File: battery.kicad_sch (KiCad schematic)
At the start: 1 part, among them U2 BQ40z50-R2

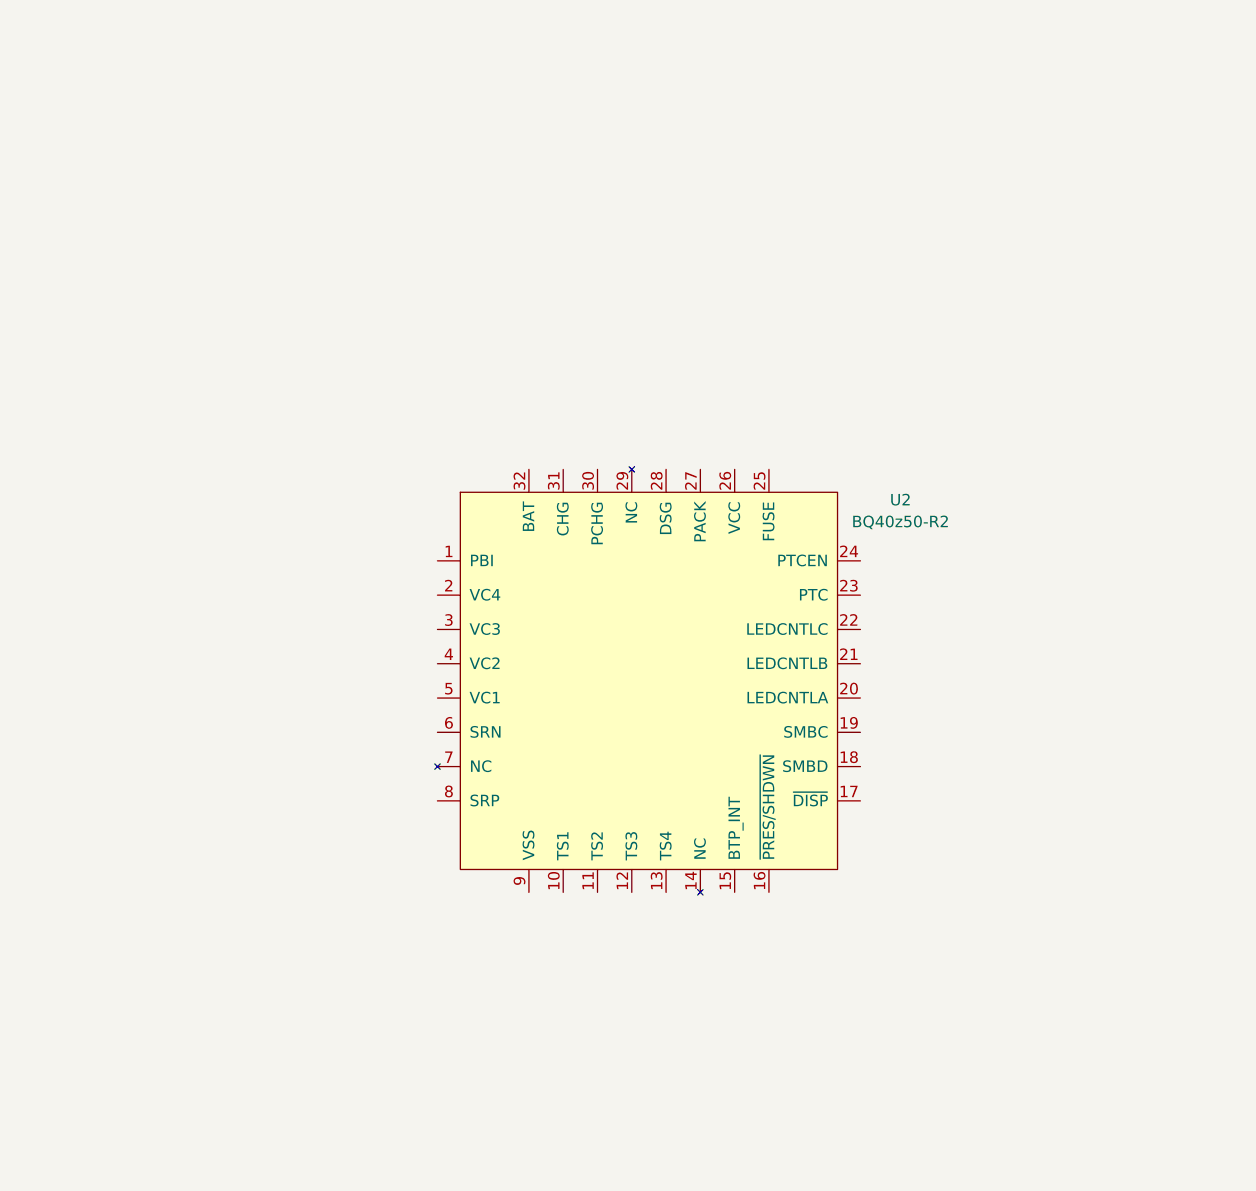
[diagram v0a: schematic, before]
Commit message: Add gauge schematic and partial charger schematic
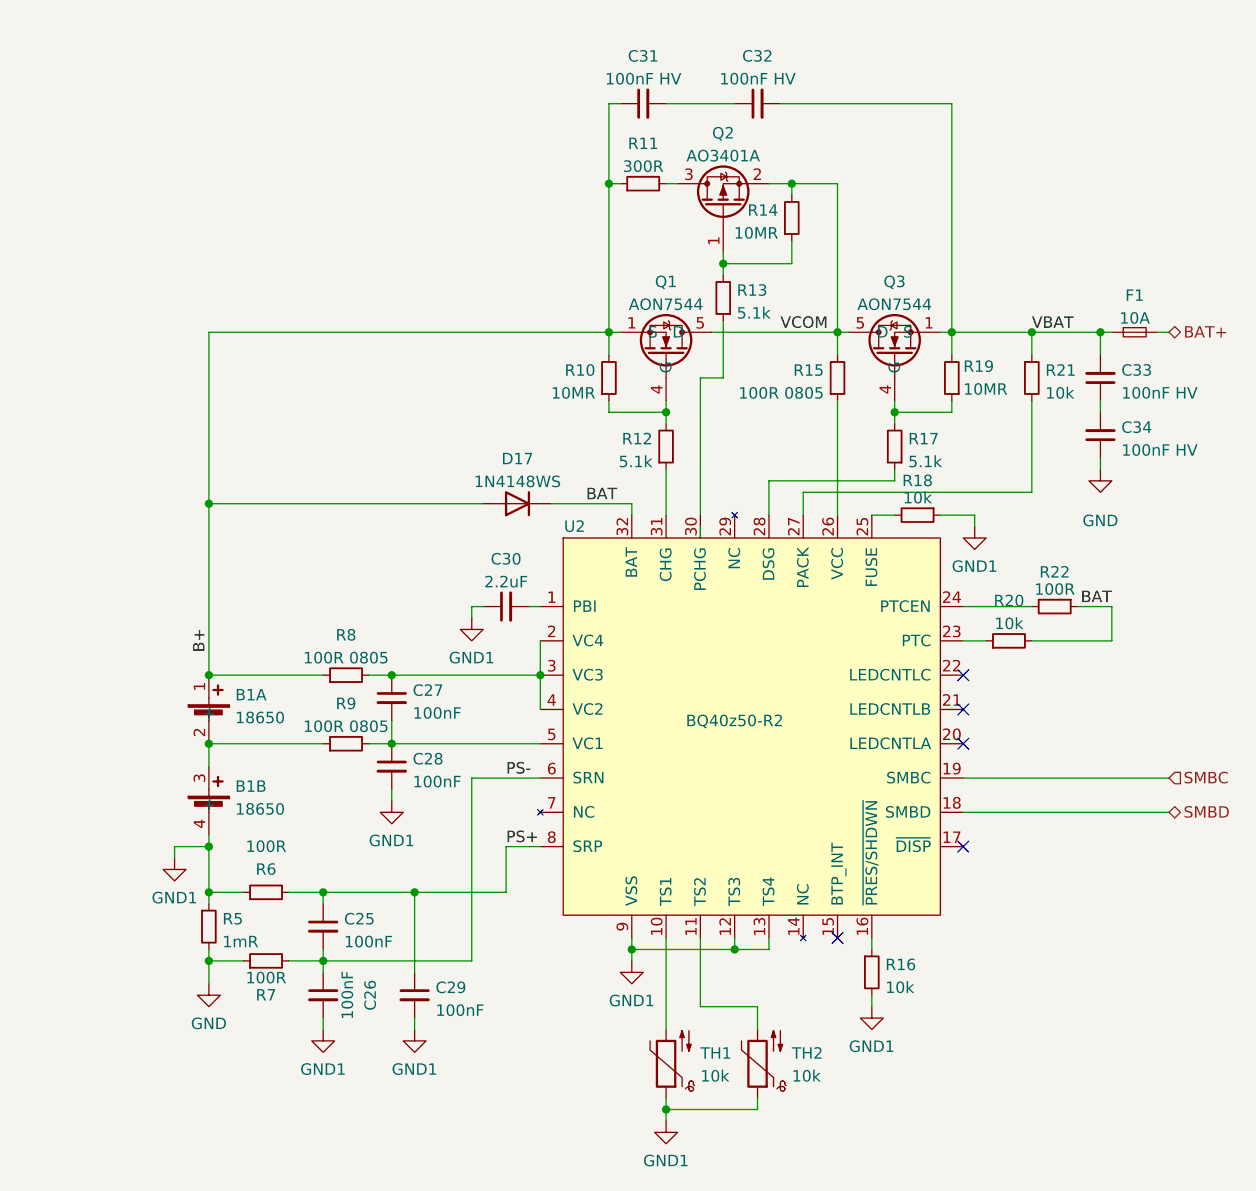
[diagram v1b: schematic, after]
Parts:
- added B1: 18650, symbol battery:battery-2s
- added C25, C26, C27, C28, C29: 100nF, Capacitor_SMD:C_0402_1005Metric, symbol Device:C_Small
- added C30: 2.2uF, Capacitor_SMD:C_0603_1608Metric, symbol Device:C_Small
- added C31, C32, C33, C34: 100nF HV, Capacitor_SMD:C_0603_1608Metric, symbol Device:C_Small
- added D17: 1N4148WS, Diode_SMD:D_SOD-323, symbol Diode:1N4148WS
- added F1: 10A, Fuse:Fuse_1206_3216Metric, symbol Device:Fuse_Small
- added Q1, Q3: AON7544, Package_DFN_FET:DFN-8-FET_3x3mm_P0.65mm, symbol Transistor_FET_DFN:AON7544
- added Q2: AO3401A, Package_TO_SOT_SMD:SOT-23, symbol Transistor_FET:AO3401A
- added R10, R14, R19: 10MR, Resistor_SMD:R_0402_1005Metric, symbol Device:R_Small
- added R11: 300R, Resistor_SMD:R_1206_3216Metric, symbol Device:R_Small
- added R12, R13, R17: 5.1k, Resistor_SMD:R_0402_1005Metric, symbol Device:R_Small
- added R15, R8, R9: 100R 0805, Resistor_SMD:R_0805_2012Metric, symbol Device:R_Small
- added R16, R18, R20, R21: 10k, Resistor_SMD:R_0402_1005Metric, symbol Device:R_Small
- added R22, R6, R7: 100R, Resistor_SMD:R_0402_1005Metric, symbol Device:R_Small
- added R5: 1mR, Resistor_SMD:R_1206_3216Metric, symbol Device:R_Small
- added TH1, TH2: 10k, Resistor_SMD:R_0402_1005Metric, symbol Device:Thermistor_NTC
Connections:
- net PWRPD is gone; now on net GND1: U2.33 (PWRPD), U2.9 (VSS)
- net at U2.1 (PBI): now also C30.2
- net at U2.10 (TS1): now also TH1.2
- net at U2.11 (TS2): now also TH2.2
- net GND1: now reaches U2.12 (TS3)
- net GND1: now also U2.13 (TS4), B1.4 (-), C26.2, C28.2, C29.2, C30.1, R16.2, R18.1, R5.1, R6.1, TH1.1, TH2.1
- net at U2.16 (~{PRES/SHDWN}): now also R16.1
- net SMBD: now reaches U2.18 (SMBD)
- net SMBC: now reaches U2.19 (SMBC)
- net at U2.2 (VC4): now also U2.3 (VC3), U2.4 (VC2), C27.1, R8.2
- net at U2.23 (PTC): now also R20.1
- net at U2.24 (PTCEN): now also R22.2
- net at U2.25 (FUSE): now also R18.2
- net at U2.26 (VCC): now also R15.1
- net at U2.27 (PACK): now also R21.2
- net at U2.28 (DSG): now also R17.1
- net at U2.30 (PCHG): now also R13.1
- net at U2.31 (CHG): now also R12.1
- net BAT: now reaches U2.32 (BAT)
- net BAT: now also D17.1 (K), R20.2, R22.1
- net at U2.5 (VC1): now also C27.2, C28.1, R9.2
- net PS-: now reaches U2.6 (SRN)
- net PS-: now also C25.2, C26.1, R7.2
- net PS+: now reaches U2.8 (SRP)
- net PS+: now also C25.1, C29.1, R6.2
- new net: C31.2, C32.1
- new net: Q2.1 (G), R13.2, R14.1
- new net: Q2.3 (D), R11.2
- new net: Q3.4 (G), R17.2, R19.1
- new net: Q1.4 (G), R10.1, R12.2
- new net: B1.2 (-), B1.3 (+), R9.1
- new net: C33.1, C34.2
- new net B+: B1.1 (+), C31.1, D17.2 (A), Q1.1 (S), Q1.2 (S), Q1.3 (S), R10.2, R11.1, R8.1
- new net BAT+: F1.2
- new net GND: C34.1, R5.2, R7.1
- new net VBAT: C32.2, C33.2, F1.1, Q3.1 (S), Q3.2 (S), Q3.3 (S), R19.2, R21.1
- new net VCOM: Q1.5 (D), Q1.6 (D), Q1.7 (D), Q1.8 (D), Q1.9 (D), Q2.2 (S), Q3.5 (D), Q3.6 (D), Q3.7 (D), Q3.8 (D), Q3.9 (D), R14.2, R15.2
- no-connect marks 0 -> 5

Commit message: Finish rough layout
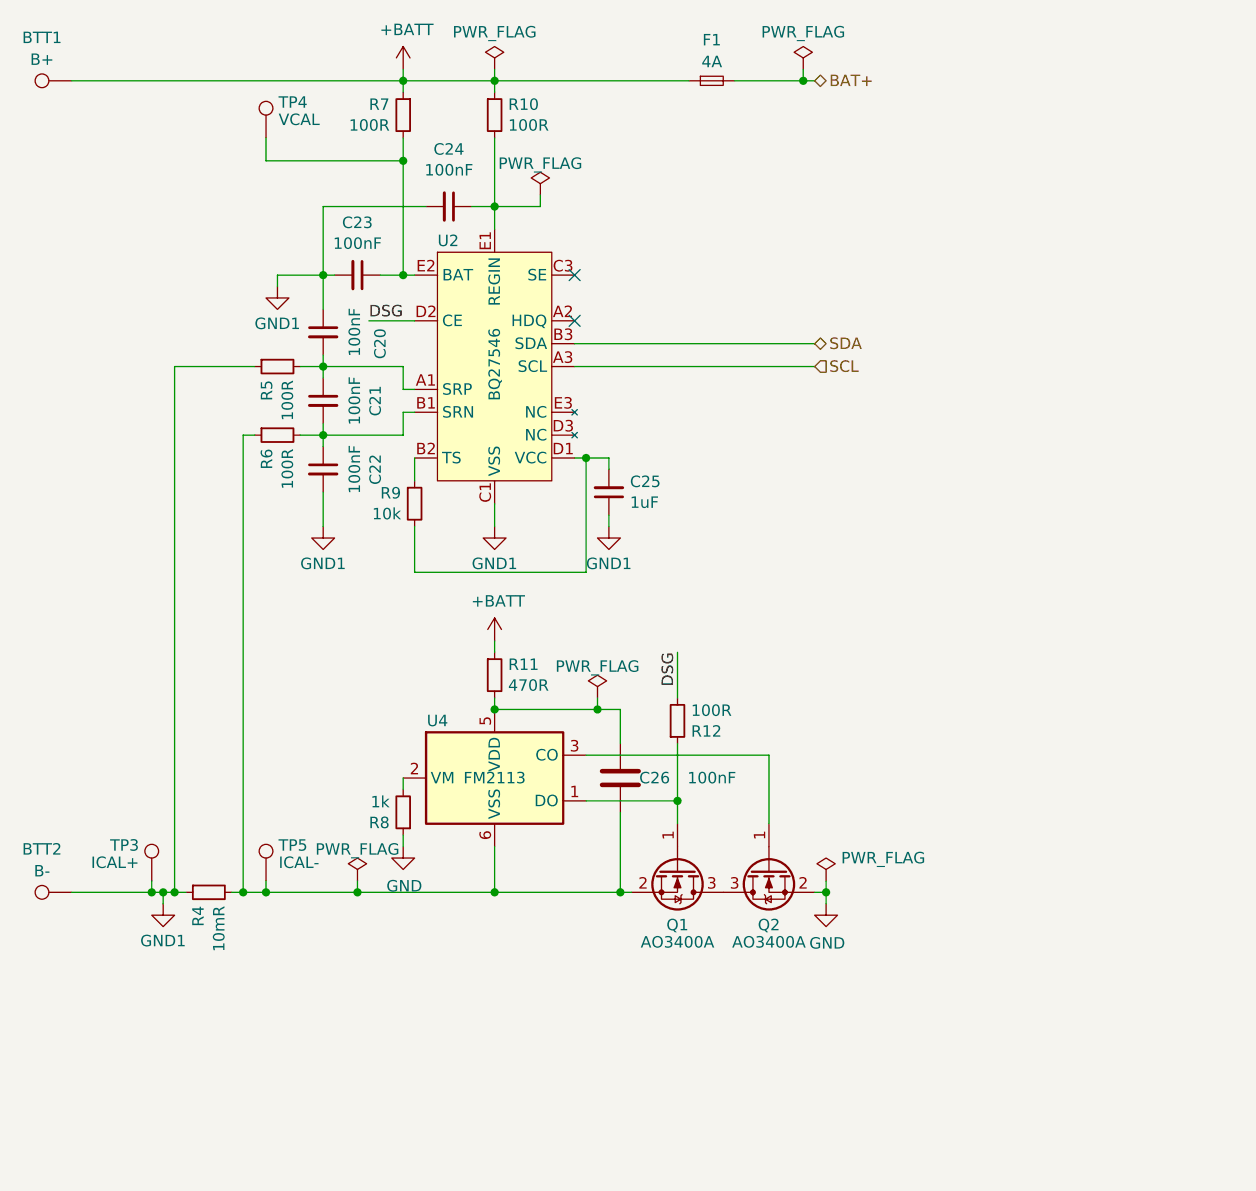
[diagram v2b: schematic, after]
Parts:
- removed B1: 18650, symbol battery:battery-2s
- removed C26, C27, C28, C29: 100nF, Capacitor_SMD:C_0402_1005Metric, symbol Device:C_Small
- removed C30: 2.2uF, Capacitor_SMD:C_0603_1608Metric, symbol Device:C_Small
- removed C31, C32, C33, C34: 100nF HV, Capacitor_SMD:C_0603_1608Metric, symbol Device:C_Small
- removed D17: 1N4148WS, Diode_SMD:D_SOD-323, symbol Diode:1N4148WS
- removed Q1, Q3: AON7544, Package_DFN_FET:DFN-8-FET_3x3mm_P0.65mm, symbol Transistor_FET_DFN:AON7544
- removed Q2: AO3401A, Package_TO_SOT_SMD:SOT-23, symbol Transistor_FET:AO3401A
- removed R13, R17: 5.1k, Resistor_SMD:R_0402_1005Metric, symbol Device:R_Small
- removed R14, R19: 10MR, Resistor_SMD:R_0402_1005Metric, symbol Device:R_Small
- removed R15: 100R 0805, Resistor_SMD:R_0805_2012Metric, symbol Device:R_Small
- removed R16, R18, R20, R21: 10k, Resistor_SMD:R_0402_1005Metric, symbol Device:R_Small
- removed R22: 100R, Resistor_SMD:R_0402_1005Metric, symbol Device:R_Small
- removed TH1, TH2: 10k, Resistor_SMD:R_0402_1005Metric, symbol Device:Thermistor_NTC
- removed U2: BQ40z50-R2, Package_Texas:VQFN-32-4.1x4.1-EP-1.4, symbol ti-balancers:BQ40z50-R2
- added BTT1: B+, Battery_Holder_MYOUNG:MY-18650-01, symbol Connector:TestPoint
- added BTT2: B-, Battery_Holder_MYOUNG:MY-18650-01, symbol Connector:TestPoint
- added C20, C21, C22, C23, C24: 100nF, Capacitor_SMD:C_0402_1005Metric, symbol Device:C_Small
- added C26: 100nF, Capacitor_SMD:C_0402_1005Metric, symbol Device:C
- added Q1, Q2: AO3400A, Package_TO_SOT_SMD:SOT-23, symbol Transistor_FET:AO3400A
- added R4: 10mR, Resistor_SMD:R_0805_2012Metric, symbol Device:R_Small
- added TP3: ICAL+, TestPoint:TestPoint_Pad_2.0x2.0mm, symbol Connector:TestPoint
- added TP4: VCAL, TestPoint:TestPoint_Pad_2.0x2.0mm, symbol Connector:TestPoint
- added TP5: ICAL-, TestPoint:TestPoint_Pad_1.5x1.5mm, symbol Connector:TestPoint
- added U2: BQ27546, Package_DSBGA:DSBGA-15_BQ27546_I2C_1.95x2.6mm_P0.5mm, symbol Fuel_Gauge_TI:BQ27546
- added U4: FM2113, Package_TO_SOT_SMD:SOT-23-6, symbol Battery_Management:AP9101CK6
- C25: value 100nF -> 1uF; LCSC C1525 -> C52923
- F1: value 10A -> 4A; LCSC C242475 -> C187596
- R10: value 10MR -> 100R; LCSC C26082 -> C25076
- R11: value 300R -> 470R; footprint Resistor_SMD:R_1206_3216Metric -> Resistor_SMD:R_0402_1005Metric; LCSC C17887 -> C25117
- R12: value 5.1k -> 100R; LCSC C25905 -> C25076
- R5: value 1mR -> 100R; footprint Resistor_SMD:R_1206_3216Metric -> Resistor_SMD:R_0402_1005Metric; LCSC C76287 -> C25076
- R8: value 100R 0805 -> 1k; footprint Resistor_SMD:R_0805_2012Metric -> Resistor_SMD:R_0402_1005Metric; LCSC C17408 -> C11702
- R9: value 100R 0805 -> 10k; footprint Resistor_SMD:R_0805_2012Metric -> Resistor_SMD:R_0402_1005Metric; LCSC C17408 -> C25744
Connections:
- net VBAT is gone; now on net +BATT: F1.1
- net GND: now also R8.1, Q2.2 (S); no longer R5.2, R7.1
- net GND1: now also C25.1, BTT2.1, C20.1, C22.2, C23.2, C24.2, R4.1, TP3.1, U2.C1 (VSS), U2.C2 (VSS); no longer R6.1
- net at R9.2: now also C25.2, U2.D1 (VCC)
- net at R11.2: now also C26.2, U4.5 (VDD)
- net +BATT: now reaches R10.1
- net +BATT: now also R11.1, R7.1, BTT1.1; no longer R12.2
- net at R9.1: now also U2.B2 (TS)
- net at R12.1: now also Q1.1 (G), U4.1 (DO)
- net at R8.2: now also U4.2 (VM)
- removed net B+: R10.2, R11.1, R8.1
- net PS+: no longer names the net of R6.2
- net PS+: now also C21.2, C22.1, U2.B1 (SRN); no longer C25.1
- net PS-: no longer names the net of R7.2
- net PS-: now also C23.1, TP4.1, U2.E2 (BAT); no longer C25.2
- new net: C26.1, Q1.2 (S), R4.2, R6.1, TP5.1, U4.6 (VSS)
- new net: C20.2, C21.1, R5.2, U2.A1 (SRP)
- new net: Q2.1 (G), U4.3 (CO)
- new net: C24.1, R10.2, U2.E1 (REGIN)
- new net: Q1.3 (D), Q2.3 (D)
- new net DSG: R12.2, U2.D2 (CE)
- new net SCL: U2.A3 (SCL)
- new net SDA: U2.B3 (SDA)
- no-connect marks 5 -> 2

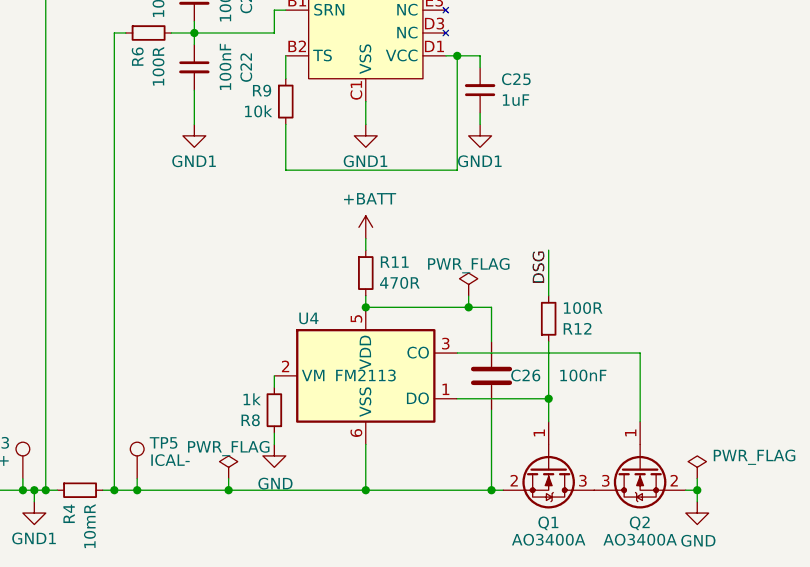
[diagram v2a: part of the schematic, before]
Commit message: Reduce battery protection IC VDD impedance
Reduce from 470R to 100R in line with manufacturers recommendation
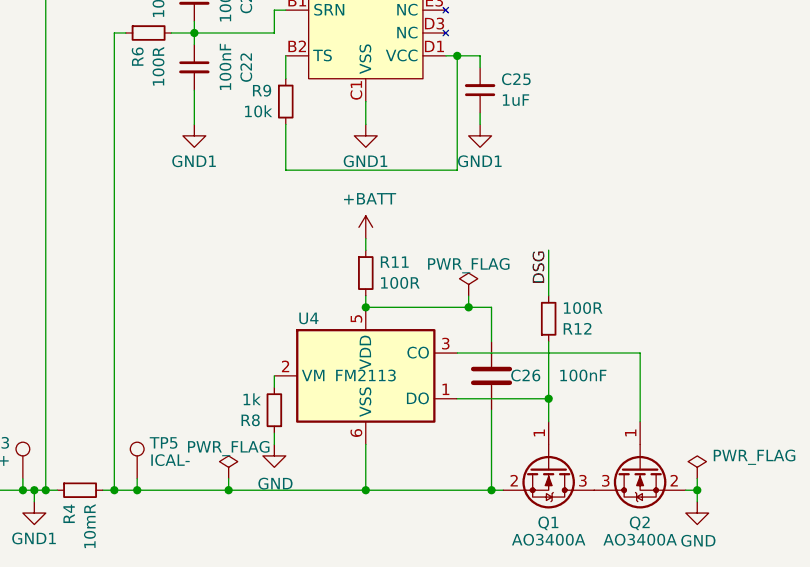
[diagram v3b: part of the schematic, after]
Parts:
- Q1, Q2: LCSC (none) -> C20917
- R11: value 470R -> 100R; LCSC C25117 -> C25076
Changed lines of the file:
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@@
       (effects (font (size 1.27 1.27)) (justify left))
     )
-    (property "Value" "470R" (at 125.9586 104.013 0)
+    (property "Value" "100R" (at 125.9586 104.013 0)
       (effects (font (size 1.27 1.27)) (justify left))
     )
@@
       (effects (font (size 1.27 1.27)) hide)
     )
-    (property "LCSC" "C25117" (at 124.46 102.87 0)
+    (property "LCSC" "C25076" (at 124.46 102.87 0)
       (effects (font (size 1.27 1.27)) hide)
     )
@@
       (effects (font (size 1.27 1.27)) (justify left) hide)
     )
+    (property "LCSC" "C20917" (at 144.78 124.46 90)
+      (effects (font (size 1.27 1.27)) hide)
+    )
     (pin "1")
     (pin "2")
@@
       (effects (font (size 1.27 1.27)) (justify left) hide)
     )
-    (pin "1")
+    (property "LCSC" "C20917" (at 154.94 124.46 90)
+      (effects (font (size 1.27 1.27)) hide)
+    )
+    (pin "1")

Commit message: battery: use flat top battery holder
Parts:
- BTT1, BTT2: footprint Battery_Holder_MYOUNG:MY-18650-01 -> Battery_Holder_MYOUNG:MY-18650-01_flat-top
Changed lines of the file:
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@@
       (effects (font (size 1.27 1.27)))
     )
-    (property "Footprint" "Battery_Holder_MYOUNG:MY-18650-01" (at 77.47 121.92 0)
+    (property "Footprint" "Battery_Holder_MYOUNG:MY-18650-01_flat-top" (at 77.47 121.92 0)
       (effects (font (size 1.27 1.27)) hide)
     )
@@
       (effects (font (size 1.27 1.27)))
     )
-    (property "Footprint" "Battery_Holder_MYOUNG:MY-18650-01" (at 77.47 31.75 0)
-      (effects (font (size 1.27 1.27)) hide)
-    )
+    (property "Footprint" "Battery_Holder_MYOUNG:MY-18650-01_flat-top" (at 77.47 31.75 0)
+      (effects (font (size 1.27 1.27)) hide)
+    )
